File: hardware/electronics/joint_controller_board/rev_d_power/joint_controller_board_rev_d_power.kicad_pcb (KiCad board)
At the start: 2 copper layers, 40 x 60 mm, 40 parts, among them J1 J_IFACE, J2 J_PWR_IN_RAW, J4 J_PWR_OUT_SW, Q1 BSC016N06NS, Q2 BSC016N06NS, U1 TPS2492PW, U2 LMR36520ADDA, U3 TLV75533PDBV

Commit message: release(rev_d_power): prepare 2oz PCBWay order state
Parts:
- moved R2 2.15 mm to (149.1, 116.1)
- moved R3 1.91 mm to (152.9, 116.1)
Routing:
- net 24V_PASS_MID: track 38.5 -> 27.1 mm, vias 5 -> 6
- net +3V3_AUX: track 11.1 -> 8.30 mm
- net PWRGD_N: track 46.9 -> 45.1 mm
- net FAULT_N: track 65.9 -> 64.3 mm

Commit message: fix(rev_d_power): swap D2 to Comchip SS56B-HF after PCBWay BOM review
PCBWay flagged Diodes Inc B560C-13-F in their quotation review: the MPN
is SMC / DO-214AB package while the PCB footprint is D_SMB / DO-214AA.
Swap to Comchip Technology SS56B-HF, a 60V / 5A Schottky in DO-214AA/SMB,
electrically equivalent (V_F, trr, I_F all match). Cathode band polarity
unchanged.

Updated in both schematic and PCB:
- Value / MPN -> SS56B-HF
- Manufacturer -> Comchip Technology
- Datasheet URL -> DigiKey SS56B-HF listing

Footprint D_SMB is preserved. No PCB layout or routing change required.
ERC and DRC remain 0/0.

Signed-off-by: graceful-kinematics <info@aliahumanoid.com>
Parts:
- D2: value B560C-13-F -> SS56B-HF
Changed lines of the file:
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@@
 			)
 		)
-		(property "Value" "B560C-13-F"
+		(property "Value" "SS56B-HF"
 			(at 0 -3.1 90)
 			(layer "B.Fab")
@@
 			)
 		)
-		(property "Datasheet" "https://www.diodes.com/assets/Datasheets/ds13005.pdf"
+		(property "Datasheet" "https://www.digikey.com/en/products/detail/comchip-technology/SS56B-HF/11584479"
 			(at 0 0 270)
 			(unlocked yes)
@@
 			)
 		)
-		(property "Description" "Negative transient clamp diode from 24V_PASS_MID to GND, 60V 5A Schottky"
+		(property "Description" "Negative transient clamp diode from 24V_PASS_MID to GND, 60V 5A Schottky, SMB/DO-214AA"
 			(at 0 0 270)
 			(unlocked yes)
@@
 			)
 		)
-		(property "Manufacturer" "Diodes Incorporated"
+		(property "Manufacturer" "Comchip Technology"
 			(at 0 0 270)
 			(unlocked yes)
@@
 			)
 		)
-		(property "MPN" "B560C-13-F"
+		(property "MPN" "SS56B-HF"
 			(at 0 0 270)
 			(unlocked yes)

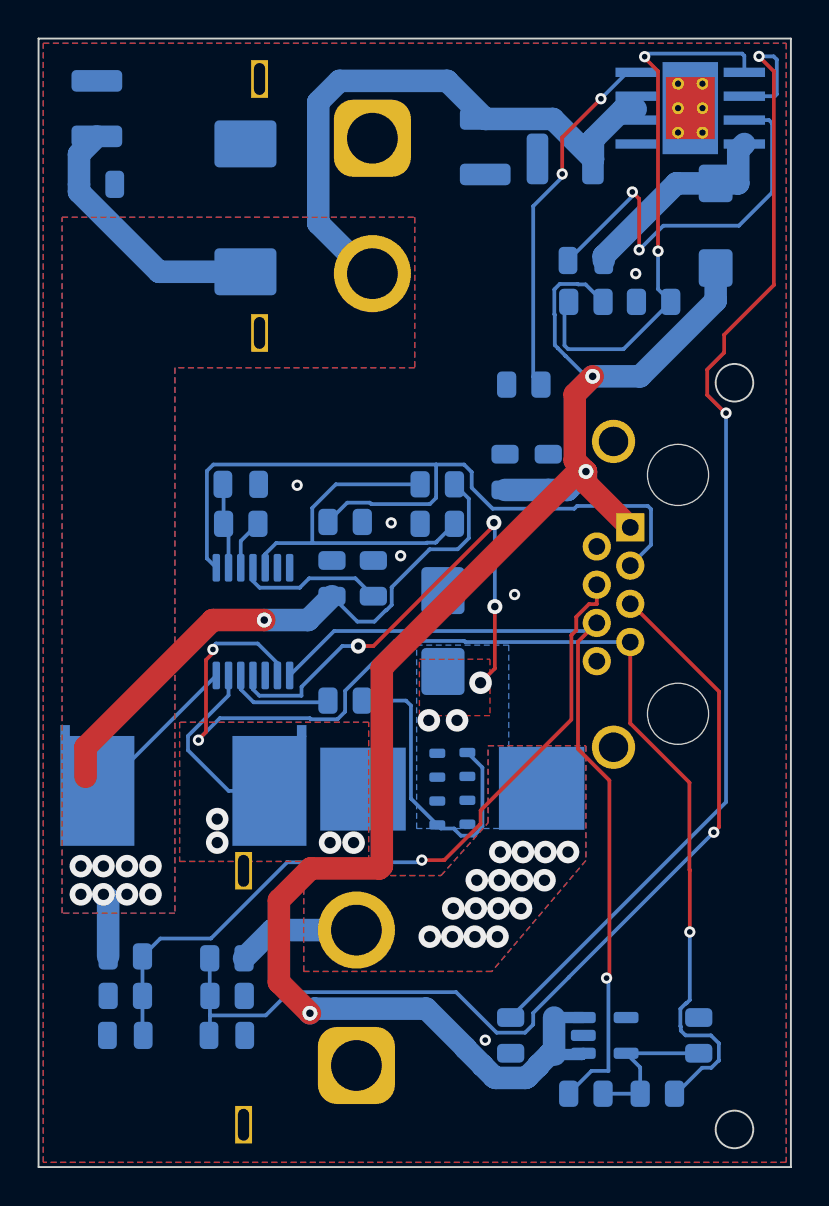
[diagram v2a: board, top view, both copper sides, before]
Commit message: hardware(rev_d_power): finalize first-lot CAD — R4 shunt substitution + local XT60 footprint library
PCBWay could not supply the originally specified R4 (WSR21L250FEA, 1.25 mOhm);
the first assembly lot uses the EQ-approved substitution WSR31L500FEA
(1.5 mOhm, 3 W Kelvin), which sets the TPS2492 current limit to Ilim ~= 33.3 A
(vs the ~40 A original design target). Schematic + PCB R4 value/MPN/description
updated accordingly.

Also migrate the J2/J4 XT60 footprints to a board-local library
(rev_d_power_footprints) whose peg-slot geometry matches the already-produced
motor_can_power_hub_rev_a, and un-ignore that library in .gitignore.

ERC 0/0, DRC 0 violations.

Signed-off-by: graceful-kinematics <info@aliahumanoid.com>
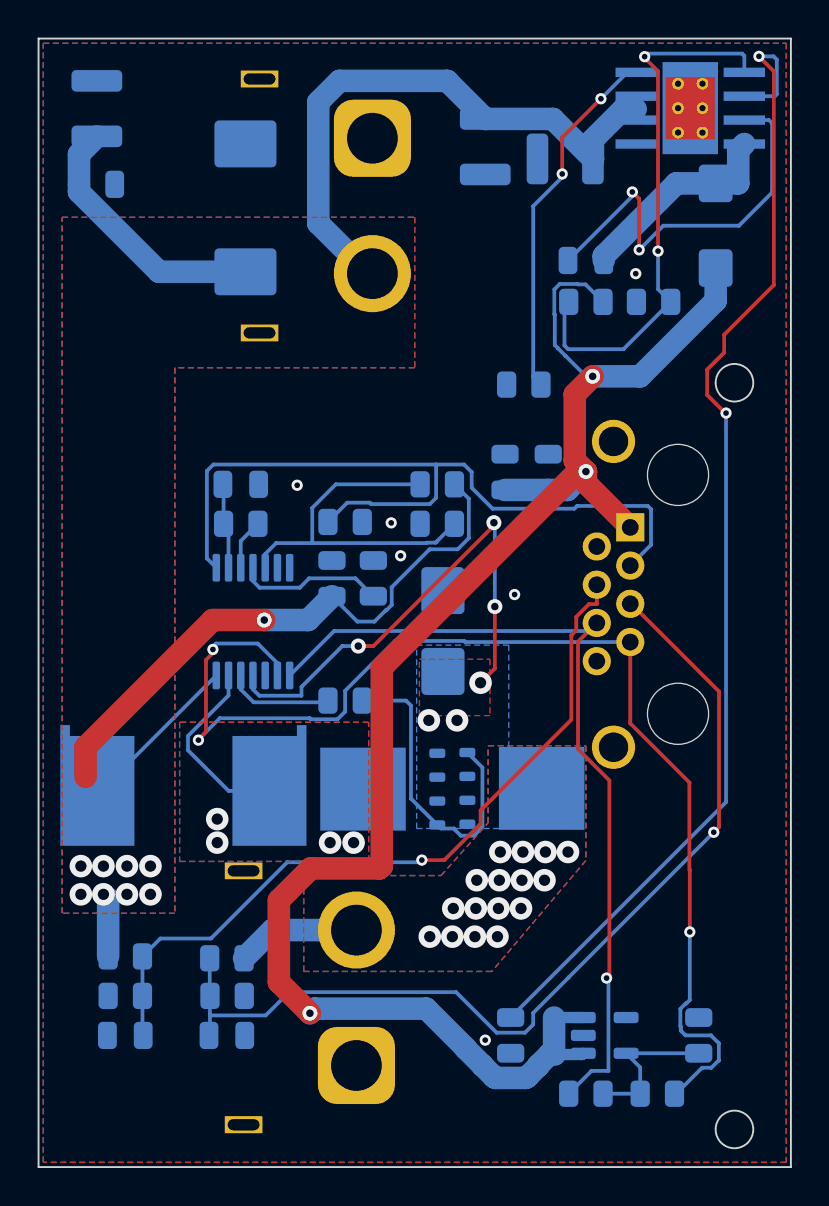
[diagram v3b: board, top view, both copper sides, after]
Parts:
- J2: footprint Connector_AMASS:AMASS_XT60PW-F_1x02_P7.20mm_Horizontal -> rev_d_power_footprints:AMASS_XT60PW-F_1x02_P7.20mm_Horizontal
- J4: footprint Connector_AMASS:AMASS_XT60PW-M_1x02_P7.20mm_Horizontal -> rev_d_power_footprints:AMASS_XT60PW-M_1x02_P7.20mm_Horizontal
- R4: value 1.25mOhm -> 1.5mOhm
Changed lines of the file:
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@@
 	(net 25 "Net-(U2-PG)")
 	(net 26 "unconnected-(U3-NC-Pad4)")
-	(footprint "Connector_AMASS:AMASS_XT60PW-M_1x02_P7.20mm_Horizontal"
+	(footprint "rev_d_power_footprints:AMASS_XT60PW-M_1x02_P7.20mm_Horizontal"
 		(layer "F.Cu")
 		(at 136.9 114.6 90)
@@
 		)
 		(pad "" thru_hole rect
-			(at -3.15 -6)
+			(at -3.15 -6 270)
 			(size 0.9 2)
 			(drill oval 0.6 1.7)
@@
 		)
 		(pad "" thru_hole rect
-			(at 10.35 -6)
+			(at 10.35 -6 270)
 			(size 0.9 2)
 			(drill oval 0.6 1.7)
@@
 		)
 	)
-	(footprint "Connector_AMASS:AMASS_XT60PW-F_1x02_P7.20mm_Horizontal"
+	(footprint "rev_d_power_footprints:AMASS_XT60PW-F_1x02_P7.20mm_Horizontal"
 		(layer "F.Cu")
 		(at 137.75 65.3 90)
@@
 		)
 		(pad "" thru_hole rect
-			(at -10.35 -6)
+			(at -10.35 -6 270)
 			(size 0.9 2)
 			(drill oval 0.6 1.7)
@@
 		)
 		(pad "" thru_hole rect
-			(at 3.15 -6)
+			(at 3.15 -6 270)
 			(size 0.9 2)
 			(drill oval 0.6 1.7)
@@
 			)
 		)
-		(property "Value" "1.25mOhm"
+		(property "Value" "1.5mOhm"
 			(at 0 -4.5 0)
 			(layer "B.Fab")
@@
 			)
 		)
-		(property "Description" "TPS2492 current-sense shunt, 1.25mOhm 1% 2W Kelvin resistor"
+		(property "Description" "TPS2492 current-sense shunt, 1.5mOhm 1% 3W Kelvin resistor; PCBWay-approved R4 substitution for first assembly lot"
 			(at 0 0 180)
 			(unlocked yes)
@@
 			)
 		)
-		(property "MPN" "WSR21L250FEA"
+		(property "MPN" "WSR31L500FEA"
 			(at 0 0 180)
 			(unlocked yes)
